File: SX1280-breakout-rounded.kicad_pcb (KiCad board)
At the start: 4 copper layers, 16 x 20.5 mm, 51 parts, among them J1 Conn_01x01, J10 Conn_01x01, J11 Conn_01x01, J12 Conn_01x01, J13 Conn_01x01, J14 Conn_01x01, J15 Conn_01x01, J16 Conn_01x01, J17 u.FL, J2 Conn_01x01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

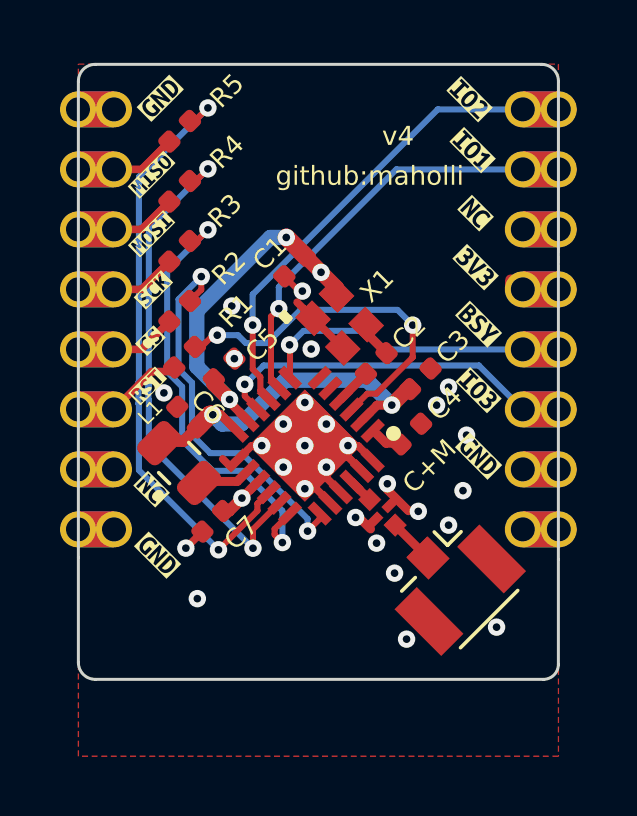
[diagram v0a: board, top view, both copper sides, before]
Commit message: back to single antenna
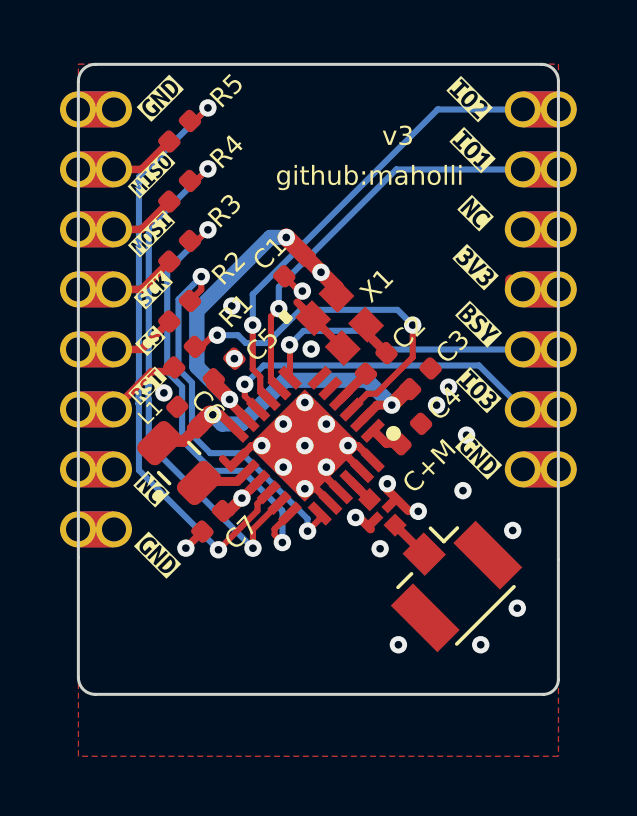
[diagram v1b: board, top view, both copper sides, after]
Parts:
- removed J9: Conn_01x01, custom-footprints:castellated_04mm
- moved REF** 0.64 mm to (107.1, 125.0)
- moved J17 0.18 mm to (111.3, 120.7)
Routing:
- net GND: vias 28 -> 27
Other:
- board size 16 x 20.5 mm -> 16 x 21 mm
- board text added: "v3"
- board text removed: "v4"
